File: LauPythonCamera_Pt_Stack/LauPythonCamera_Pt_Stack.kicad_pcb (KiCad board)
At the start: 4 copper layers, 55 x 45 mm, 68 parts, among them J1 DF40C-80DP (Bank A), J2 DF40C-80DP (Bank B), J3 DF40C-50DP (Control), U1 NOIP1SN1300A-QDI, U2 TPS7A2018PDBVR, U3 TPS61023DRLR, U4 TPS7A2033PDBVR, U5 TPS7A2033PDBVR, U6 TLV803SDBZT, U7 TLV803SDBZT

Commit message: hw(camera): route all 7 LVDS pairs -- zero intra-pair skew by construction
Socket -> Bank B, 720 Mbps data + 360 MHz clocks. 92 tracks, 38 vias.
DRC: 0 clearance, 0 shorts, 0 track-width, 0 diff-pair, 0 uncoupled.

TWO-LAYER MANHATTAN FAN, not a diagonal. The bundle shifts right up to 7.08 mm
while dropping ~5 mm, so any diagonal is shallow -- and a pair offset 0.44 mm
along X at 13.5 deg has a PERPENDICULAR separation of only 0.44*sin(13.5) =
0.10 mm. The legs merge. A first attempt did exactly that and DRC found 15
shorts. Down/across/down keeps the offset perpendicular to travel at all times,
so the gap is always 0.44 mm. Six pairs need ~5.3 mm of horizontal lanes and the
corridor is 6.14 mm, so three pairs fan on B.Cu and three on F.Cu.

SKEW IS ZERO BY CONSTRUCTION, NOT TUNED. At each 90 deg corner the inner leg is
short by exactly the pair pitch and the outer leg is long by the same; the route
turns once each way, so the errors cancel. All 7 pairs measure 0.0000 mm.

R2 -> B.Cu. Sensor pins 23/24 are on the socket's RIGHT edge and both escape
LEFT; the pair arrives from BELOW and R2 must bridge them. On F.Cu that always
crosses -- the inner leg's vertical lies across the outer leg's path to R2. On
B.Cu the pair's legs sit side by side in X, so a horizontal R2 straddles them and
the bridge is on a different layer from the pin escapes. Costs nothing: the three
DF40s are already bottom-side. (It also needed rot 180 -- after the flip pad 1
carried _P, and N comes up the channel on the left.)

lvds_clock_in needed 1.816 mm of length compensation, and it is STRUCTURAL:
pin 24 (P) sits 1.016 mm further along AND its via is 0.8 mm further right, so
P is longer by exactly (1.016 + 2*splay) for ANY via position -- the mirror
topology gives the same magnitude with the sign flipped. N carries a 0.908 mm
out-and-back on B.Cu that cancels it exactly.

DRC RULES -- read the .kicad_dru comments before "simplifying" any of these:

* DF40 fanout neck-down. THE TWO CamLVDS RULES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
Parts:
- R2: moved to B.Cu
- moved R2 0.10 mm to (148.1, 83.0), turned to 180 degrees
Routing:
- net CAM_LVDSCLK_P: track 0.00 -> 24.1 mm, vias 0 -> 1
- net CAM_LVDSCLK_N: track 0.00 -> 24.1 mm, vias 0 -> 1
- net GND: vias 28 -> 24

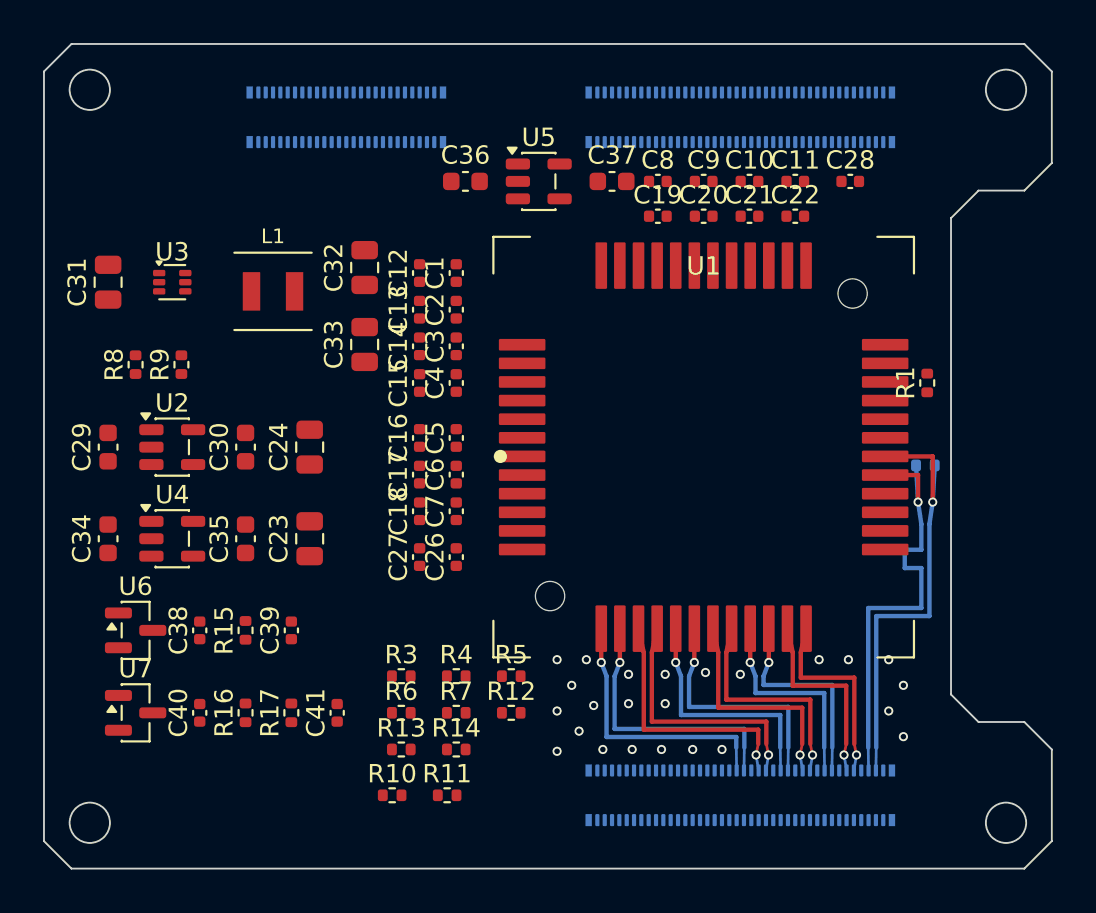
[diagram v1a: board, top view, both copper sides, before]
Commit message: feat(camera-pcb): autoroute power/control + add GND pours on PYTHON 1300 board
Layout was placement + LVDS-only. Completed the power/control routing and
ground connection, leaving the hand-routed LVDS untouched.

- Autorouted the power and control nets with Freerouting, driven off a
  Specctra DSN with the 7 LVDS pairs + GND stitching locked as fixed wiring.
  Merged the session back LVDS-safe: purge any LVDS-net copper the import
  introduced and re-add the original pairs verbatim -- all 14 net lengths
  verified byte-identical to the hand route (CLKOUT 14.873, LVDSCLK 24.054...).
- Added F.Cu + B.Cu GND pours and refilled the In1/In2 planes, connecting the
  bulk of GND and carving via antipads. Ratsnest 237 -> 27.
- New DRU rule: hold the B.Cu GND pour >=0.5mm off the LVDS pairs so the 100R
  geometry stays edge-coupled microstrip over In2, not coplanar waveguide.

Remaining (to finish by hand in the GUI): ~23 power/control stragglers
Freerouting could not thread around the fixed LVDS + 0.4mm connectors, 4 stray
GND pads, and DRC cleanup (sub-min track widths, starved thermals, dangling
stubs, pre-existing silk overlaps).

Co-Authored-By: Claude Opus 4.8 (1M context) <noreply@anthropic.com>
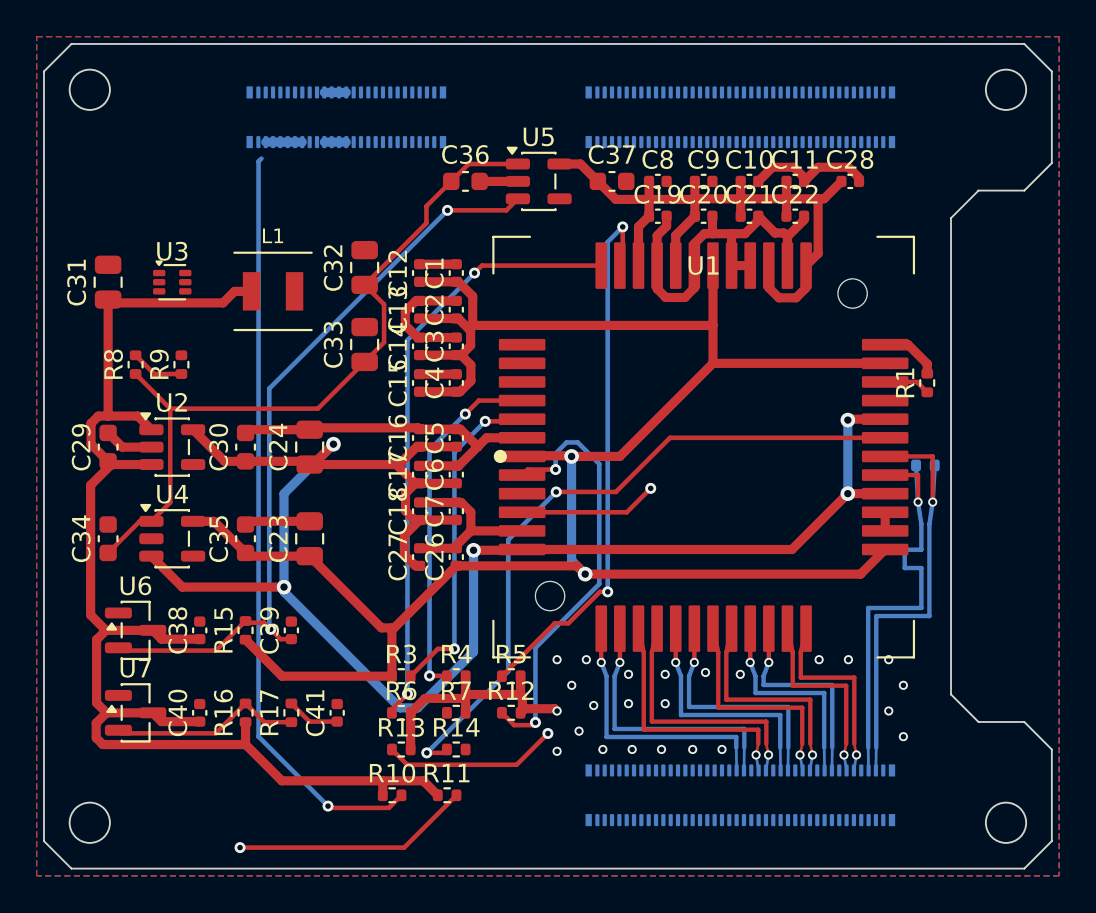
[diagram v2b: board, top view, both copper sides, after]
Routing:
- net +3V3_CAM: track 0.00 -> 117.5 mm, vias 0 -> 2
- net GND: track 0.00 -> 98.8 mm
- net +1V8_CAM: track 0.00 -> 95.7 mm, vias 0 -> 5
- net +3V3_SYS: track 0.00 -> 74.0 mm
- net EN_PIX: track 0.00 -> 41.6 mm, vias 0 -> 2
- net VBSEL_A: track 0.00 -> 41.3 mm, vias 0 -> 1
- net +4V5: track 0.00 -> 40.7 mm
- net +3V3_PIX: track 0.00 -> 39.1 mm
- net CAM_CLK_PLL: track 0.00 -> 37.5 mm, vias 0 -> 2
- net CAM_TRIG1: track 0.00 -> 33.0 mm, vias 0 -> 2
- net CAM_TRIG0: track 0.00 -> 31.3 mm, vias 0 -> 2
- net CAM_MOSI: track 0.00 -> 23.7 mm, vias 0 -> 2
- net CAM_RESET_N: track 0.00 -> 19.5 mm, vias 0 -> 2
- net CAM_SS_N: track 0.00 -> 18.2 mm, vias 0 -> 2
- net CAM_SCK: track 0.00 -> 17.1 mm, vias 0 -> 2
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- added copper zone on B.Cu, net GND
- added copper zone on F.Cu, net GND

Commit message: feat(camera-pcb): complete control + power routing on PYTHON 1300 board
Finishes the physical layout: all 11 single-ended control nets and the
power tree are now routed alongside the previously-done LVDS pairs and GND
planes. Board is DRC-clean apart from the documented LVDSCLK splay.

- Control (MOSI/MISO/SCK/SS_N/CLK_PLL/RESET_N/TRIG0-2/MON0-1): routed
  sensor -> J1 Bank A. The sensor->connector pin mapping is a reversed
  permutation, so the fanout was threaded interactively (shove-router) with
  per-crossing layer hops -- 0 shorts, 0 crossings.
- Pull-resistors R3-R7,R12-R14 relocated adjacent to their control signals
  (short stubs) to make the fanout routable; +3V3_PIX caps left in place.
- Power tree (+3V3_SYS/+4V5/SW/+1V8_CAM/+3V3_CAM/+3V3_PIX + EN/FB/RST
  supervisors + VBSEL straps) routed; all +3V3_SYS input pins tied.
- GND: In1/In2 solid planes + F.Cu/B.Cu pours (solid pad connection) +
  stitching. One redundant connector pad (J1.2) left unbonded on this side
  (its neighbour J1.1 and the planes carry the return) -- cosmetic ratsnest.
- DRU: scoped the "DF40 fanout neck-down track width" rule to non-power nets
  so wide power/GND traces near the connectors are no longer flagged; the
  neck-down still holds the fine LVDS + control escapes. Added a B.Cu GND
  pour >=0.5mm keep-off from the LVDS pairs to preserve microstrip Zdiff.

Remaining DRC: 3 CAM_LVDSCLK diff-pair items (the geometrically-forced
clock splay at R2, documented in the .kicad_dru).

Co-Authored-By: Claude Opus 4.8 (1M context) <noreply@anthropic.com>
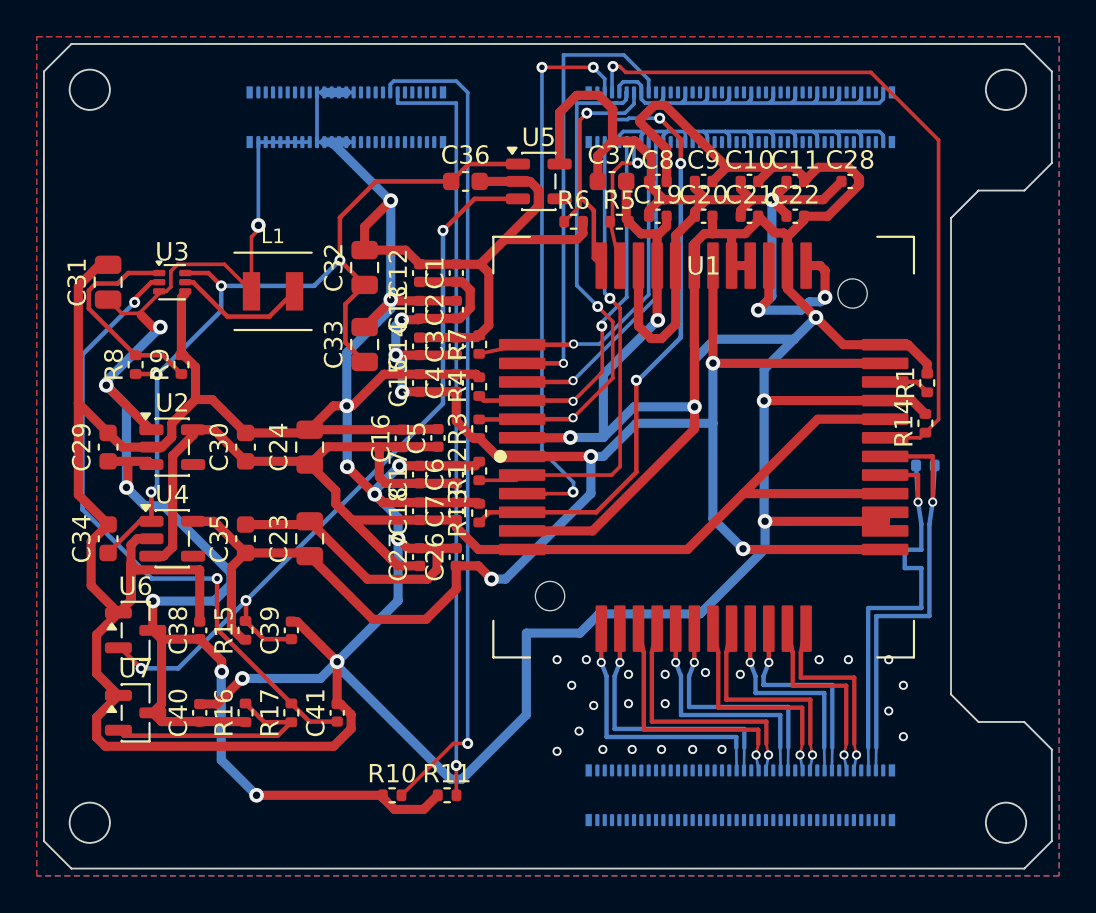
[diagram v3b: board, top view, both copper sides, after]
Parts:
- moved R14 31.2 mm to (148.1, 80.7), turned to 90 degrees
- moved R6 28.4 mm to (128.9, 69.7)
- moved R5 25.5 mm to (131.4, 69.7)
- moved R7 20.1 mm to (123.8, 76.4), turned to 90 degrees
- moved R4 15.8 mm to (123.8, 78.7), turned to 90 degrees
- moved R3 14.2 mm to (123.8, 81.0), turned to 90 degrees
- moved R13 13.6 mm to (123.8, 85.6), turned to 90 degrees
- moved R12 13.3 mm to (123.8, 83.3), turned to 90 degrees
- moved C5 1.00 mm to (121.5, 81.5)
- moved C16 0.95 mm to (119.5, 81.5)
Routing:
- net GND: track 98.8 -> 437.4 mm, vias 24 -> 38
- net CAM_MISO: track 0.00 -> 32.4 mm, vias 0 -> 3
- net EN_BOOST: track 2.91 -> 34.7 mm, vias 0 -> 2
- net VBSEL_B: track 13.0 -> 41.6 mm
- net CAM_MON0: track 0.00 -> 25.0 mm, vias 0 -> 1
- net +3V3_PIX: track 39.1 -> 62.6 mm, vias 0 -> 3
- net CAM_TRIG0: track 31.3 -> 8.00 mm, vias 2 -> 1
- net CAM_TRIG1: track 33.0 -> 14.1 mm, vias 2 -> 1
- net CAM_TRIG2: track 0.00 -> 18.8 mm, vias 0 -> 1
- net CAM_MON1: track 0.00 -> 17.7 mm, vias 0 -> 1
- net +1V8_CAM: track 95.7 -> 78.2 mm, vias 5 -> 0
- net CAM_SCK: track 17.1 -> 34.4 mm, vias 2 -> 3
- net +3V3_SYS: track 74.0 -> 87.8 mm, vias 0 -> 7
- net +3V3_CAM: track 117.5 -> 104.5 mm, vias 2 -> 7
- net CAM_SS_N: track 18.2 -> 27.3 mm
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
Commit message: docs(camera): sensor part is NOIP1SN1300A-QTI (-QDI discontinued)
DigiKey/onsemi have discontinued the -QDI suffix; -QTI is the identical
PYTHON 1300 LVDS sensor that ships with a peel-off protective foil over the
glass (remove before install; its tab conveniently points to pin 1).

Updated the part number in README (§4 ordering note, §12 assembly note, open
item #1), CAMERA_SENSOR_PROTOCOL.md, the schematic + PCB U1 value field, and
both BOM CSVs. Left the eval-kit SKU (NOIP1SN1300A-QDI-A-GEVK) unchanged --
that's a separate product. Value-field only; no layout/netlist change.

Co-Authored-By: Claude Opus 4.8 (1M context) <noreply@anthropic.com>
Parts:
- U1: value NOIP1SN1300A-QDI -> NOIP1SN1300A-QTI
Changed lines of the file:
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@@
 			)
 		)
-		(property "Value" "NOIP1SN1300A-QDI"
+		(property "Value" "NOIP1SN1300A-QTI"
 			(at 0 9.882 0)
 			(layer "F.Fab")

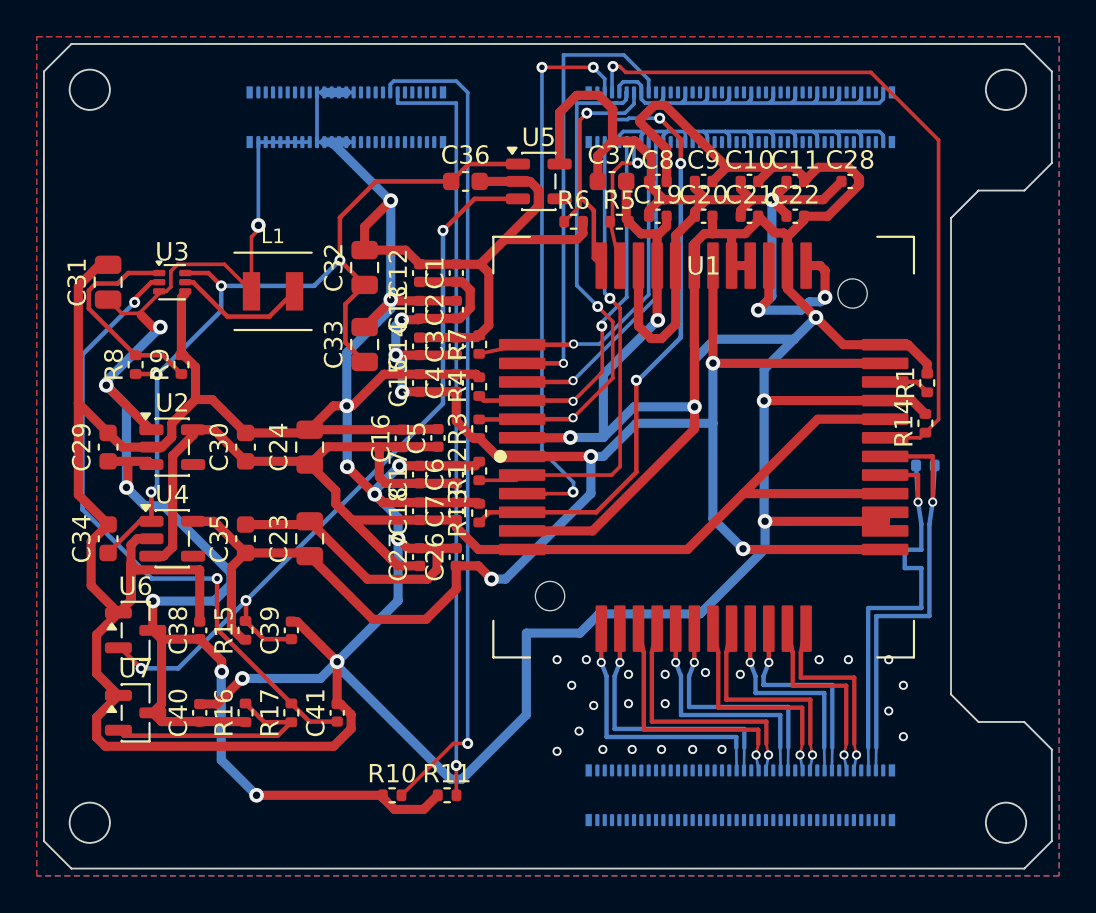
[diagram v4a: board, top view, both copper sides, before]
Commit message: fix(camera): correct L1 SMNR4020 land pattern + tie J1 GND islands; regen production
JLCPCB flagged L1's footprint as a package mismatch on order SMT026071660032_Y5.
Root cause was a misread of SXN's own drawing, not a wrong part: the SMNR4020-2.2UH
(LCSC C135262) is correct. On the datasheet's Recommended Land Pattern, F=0.95 is
each pad's SHORT side, G=2.1 is the GAP between pads, and H=3.3 is each pad's LONG
side. The footprint had used G as pad width and H as the outer span, giving 0.95 x
2.1 pads at +/-1.175 -- ~40% too little solder area on the highest-current part.

  - L1 land corrected to 0.95 x 3.3 pads at +/-1.525 (span 4.0, gap 2.1), matching
    all four datasheet dims. Fixed in the .kicad_mod and the board's embedded copy;
    descr rewritten to record what F/G/H mean so it can't be re-misread.
  - L1 rotated 180 and repositioned so SW faces U3 (shorter switch-node loop);
    +3V3_SYS re-fed from the existing via. (Routing done in the GUI.)
  - J1 pins 1 and 2 (both GND) were on isolated B.Cu pour islands, unconnected to
    the plane -- same failure mode as the rev-1 CamTrigger GND island. Pin 1 merged
    into the main pour; pin 2 tied down with a stitching via. DRC now 0 unconnected.
  - Two dangling via stubs (CAM_RESET_N, CAM_SS_N) removed.
  - Production regenerated: gerbers, drill, CPL, gerbers.zip. BOM unchanged
    (byte-identical) -- only L1's geometry moved, not its part.
  - Dropped the duplicate production/bom.csv; keep the JLC-named _bom.csv.

Remaining DRC: 4 errors, all at the LVDS clock right-edge fanout (diff-pair gap,
uncoupled length, 0.9 ps skew) -- geometrically forced at the 0.4mm pitch, per the
DRU note; not fab blockers. Reply to JLCPCB: option C (redesign footprint).

Co-Authored-By: Claude Opus 4.8 (1M context) <noreply@anthropic.com>
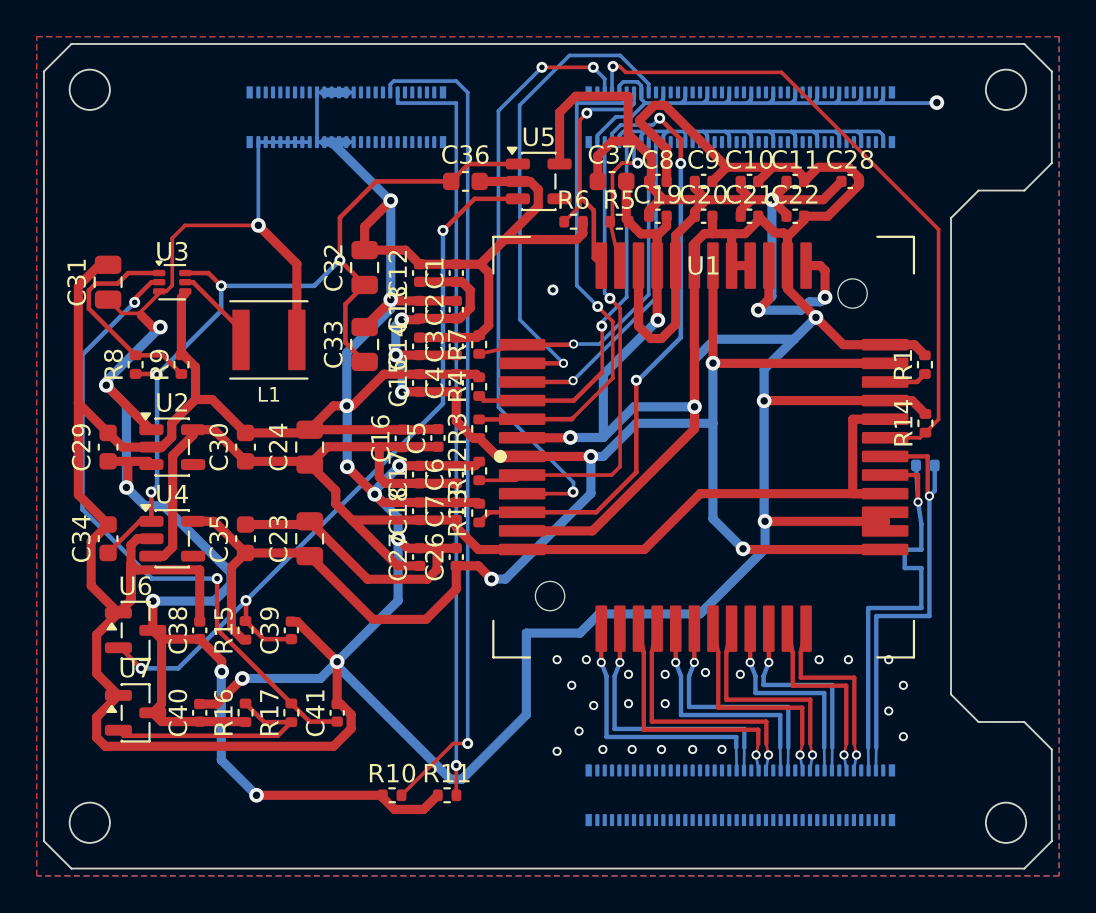
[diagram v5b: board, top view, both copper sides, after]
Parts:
- moved L1 2.66 mm to (112.3, 76.2), turned to 180 degrees
- moved R1 1.01 mm to (148.1, 77.5)
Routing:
- net GND: track 437.4 -> 443.4 mm, vias 38 -> 40
- net +3V3_SYS: track 87.8 -> 92.8 mm
- net CAM_CLK_PLL: track 39.4 -> 36.6 mm
- net SW: track 7.31 -> 4.66 mm
- net CAM_MISO: track 32.4 -> 34.4 mm
- net +1V8_CAM: track 78.2 -> 76.4 mm
- net CAM_MON0: track 25.0 -> 26.6 mm
- net +3V3_PIX: track 62.6 -> 63.9 mm
- net CAM_SS_N: track 27.3 -> 27.2 mm, vias 2 -> 1
- net CAM_RESET_N: vias 2 -> 1
